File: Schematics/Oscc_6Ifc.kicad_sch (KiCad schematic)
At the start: 101 parts

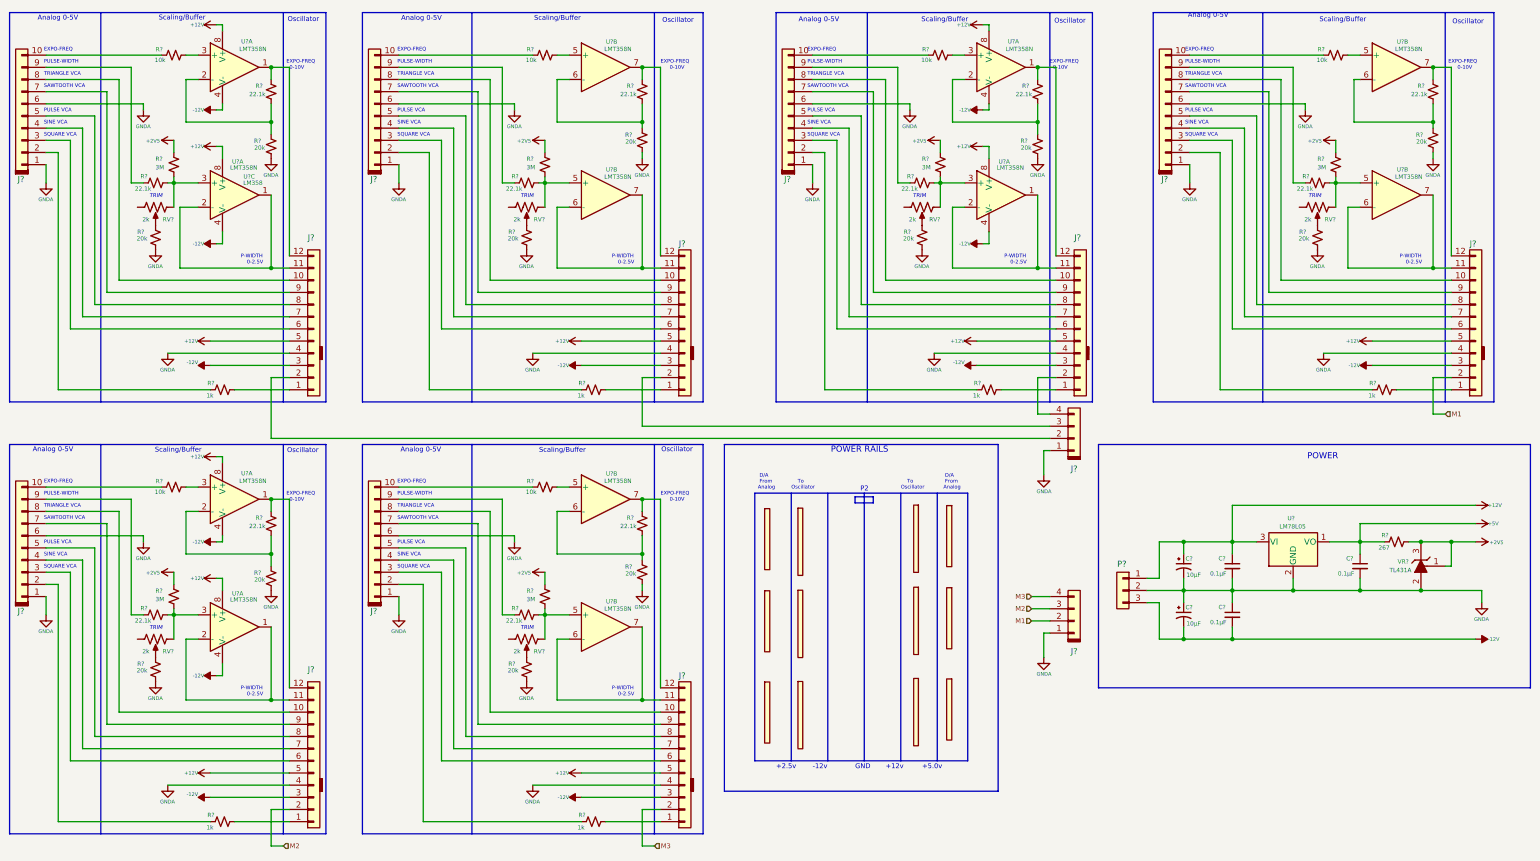
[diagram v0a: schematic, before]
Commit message: - Updated current libraries - New 7 inc display with ESP32S3 and second USB upload port - Start of I2C feeder interface slave on display.
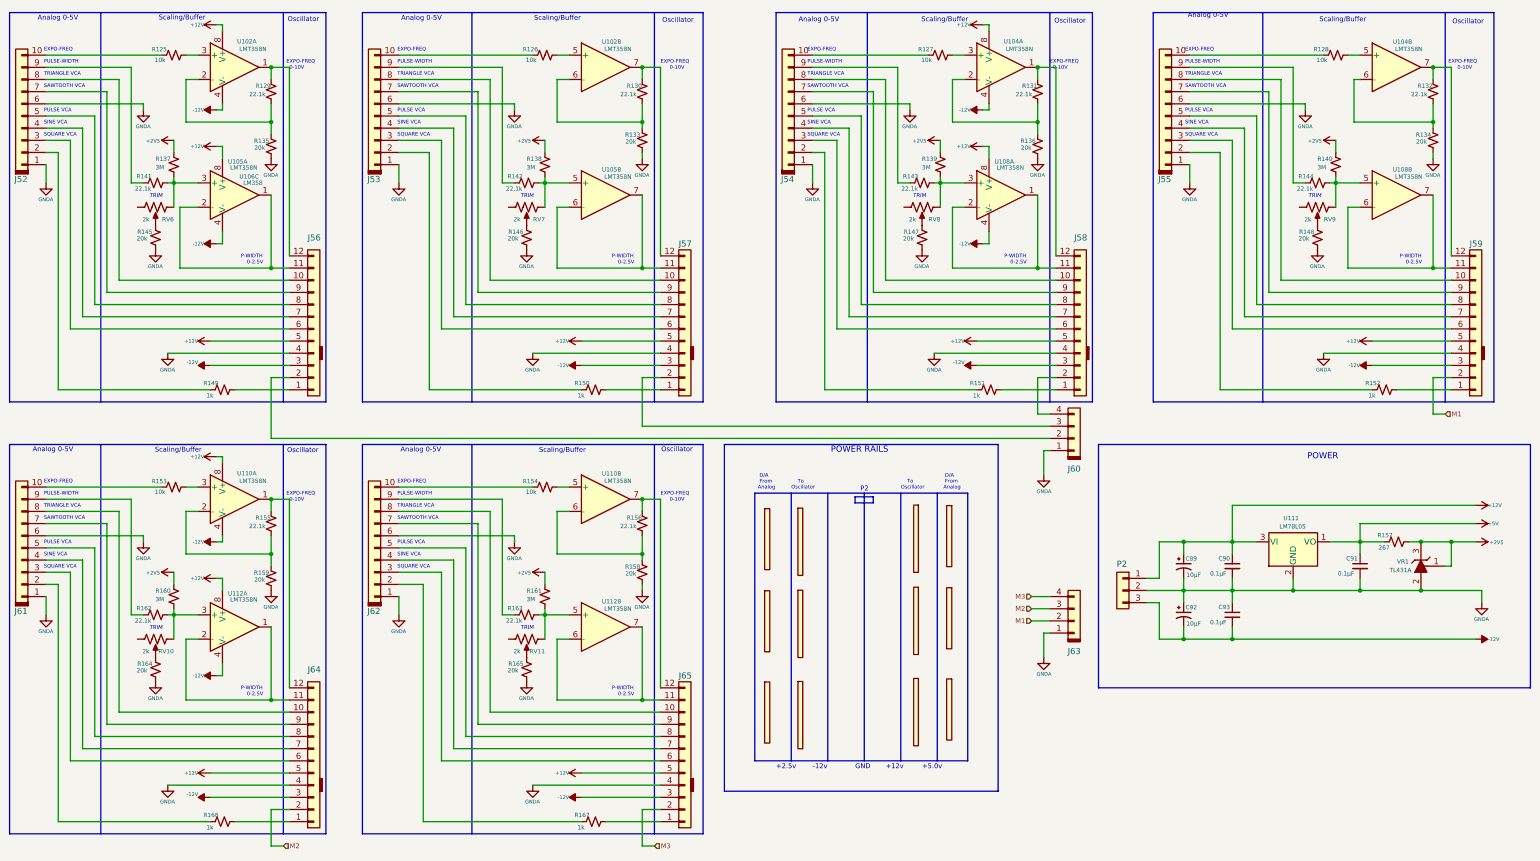
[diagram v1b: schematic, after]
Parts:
- gave numbers to parts that had none: 95
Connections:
- net at RV6. (3): now also R145.1
- net at RV7. (3): now also R146.1
- net at RV8. (3): now also R147.1

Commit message: working interface for 7 inch display with occasional faults.
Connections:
- net at RV6. (3): now also R145.1
- net at RV7. (3): now also R146.1
- net at RV8. (3): now also R147.1
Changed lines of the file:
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@@
 	)
 	(symbol
-		(lib_name "Device:R_Potentiometer_US")
 		(lib_id "Device:R_Potentiometer_US")
 		(at 50.8 59.69 270)
@@
 	)
 	(symbol
-		(lib_name "Device:R_Potentiometer_US")
 		(lib_id "Device:R_Potentiometer_US")
 		(at 128.27 59.69 270)
@@
 	)
 	(symbol
-		(lib_name "Device:R_Potentiometer_US")
 		(lib_id "Device:R_Potentiometer_US")
 		(at 50.8 149.86 270)
@@
 	)
 	(symbol
-		(lib_name "Device:R_Potentiometer_US")
 		(lib_id "Device:R_Potentiometer_US")
 		(at 128.27 149.86 270)
@@
 	)
 	(symbol
-		(lib_name "Device:R_Potentiometer_US")
 		(lib_id "Device:R_Potentiometer_US")
 		(at 210.82 59.69 270)
@@
 	)
 	(symbol
-		(lib_name "Device:R_Potentiometer_US")
 		(lib_id "Device:R_Potentiometer_US")
 		(at 293.37 59.69 270)
